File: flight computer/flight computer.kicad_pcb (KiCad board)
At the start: 4 copper layers, 43.2 x 99.1 mm, 153 parts, among them IC1 AT25SF128A-SHB-T, IC2 114993390, IC3 ADXL375BCCZ-RL, J1 JST, J10 Micro_SD_Card, J11 pyro 1, J12 pyro 2, J13 pyro 3, J14 pyro 4, J15 motor out, J16 5V out, J17 motor in, J18 servo 1, J19 servo 2, J2 battery in, J20 servo 3, J21 servo 4, J22 SMA-J-P-H-ST-EM1, J23 SMA-J-P-H-ST-EM1, J3 battery sw, J4 pyro sw, J5 12V out, J6 5V out, J7 3.3V out, J8 USB_C_Receptacle_USB2.0_16P, J9 GPIO, Q3 SIA440DJ-T1-GE3, Q4 SIA440DJ-T1-GE3, Q5 SIA440DJ-T1-GE3, Q6 SIA440DJ-T1-GE3, U1 RP2350B, U10 MAX-M10S-00B, U4 AZ1117CH-3.3TRG1, U5 TPS56A37RPAR, U6 SISS65DN-T1-GE3, U7 BTM9011EP, U8 BMP581, U9 BNO086, Y1 ABM8-272-T3

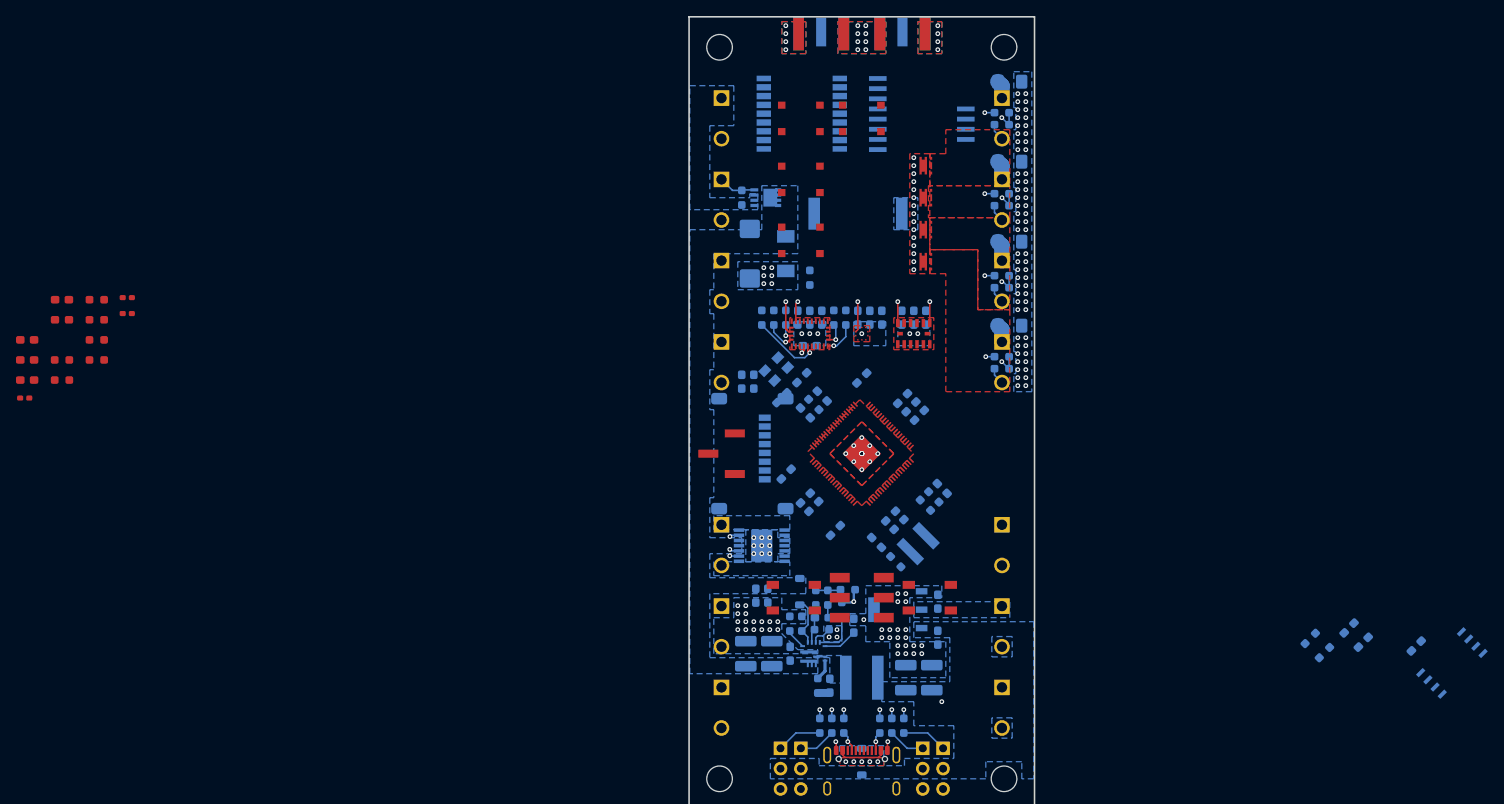
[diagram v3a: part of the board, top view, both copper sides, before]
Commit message: Microcontroller power complete
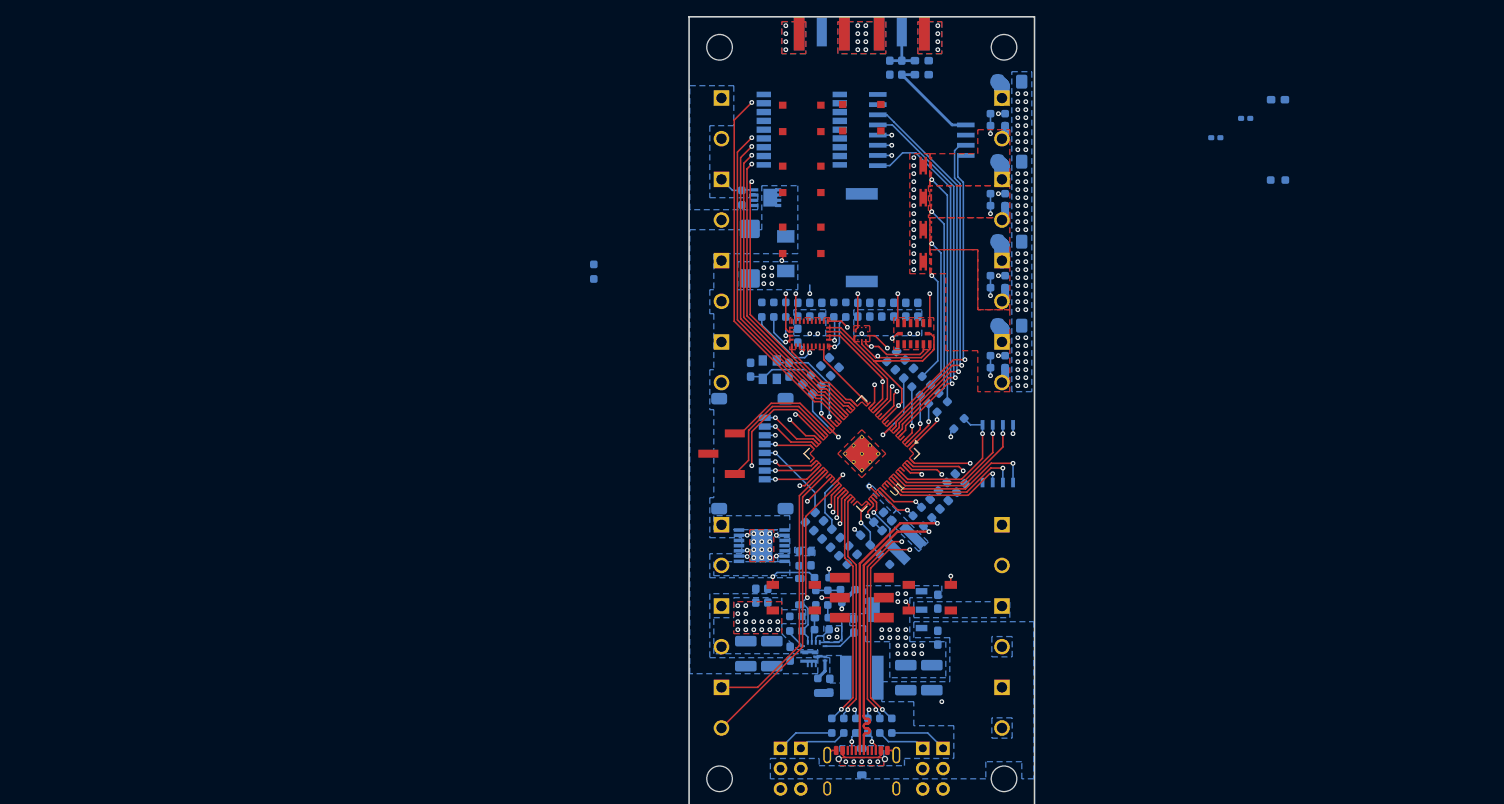
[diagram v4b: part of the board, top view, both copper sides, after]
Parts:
- removed CR3: PESD0402-140, Inductor_SMD:L_0402_1005Metric_Pad0.77x0.64mm_HandSolder
- added D1: D_TVS, Diode_SMD:D_0603_1608Metric_Pad1.05x0.95mm_HandSolder, B.Cu at (201.9, 40.6)
- C40, C43, C52, C54, CR2, L3, L4, R22, R42, R45, R46, R47, R48: moved to B.Cu
- U1: footprint Package_DFN_QFN:QFN-80-1EP_10x10mm_P0.4mm_EP3.4x3.4mm -> Package_DFN_QFN:QFN-80-1EP_10x10mm_P0.4mm_EP3.4x3.4mm_ThermalVias
- Y1: footprint Samacsys:ABM8272T3 -> Snapeda:XTAL_ABM8-272-T3
- moved C43 159.7 mm to (250.4, 44.7), turned to 180 degrees
- moved CR2 156.6 mm to (246.4, 47.0), turned to 180 degrees
- moved R42 154.0 mm to (250.4, 54.7), turned to 180 degrees
- moved L3 137.8 mm to (242.6, 49.4), turned to 180 degrees
- moved C52 118.2 mm to (205.9, 41.5)
- moved C54 111.6 mm to (205.9, 39.8)
- moved L4 109.6 mm to (203.4, 40.6), turned to 90 degrees
- moved R45 106.5 mm to (208.4, 83.0), turned to 45 degrees
- moved R46 105.1 mm to (207.4, 82.0), turned to 45 degrees
- moved R47 103.8 mm to (206.3, 81.0), turned to 45 degrees
- moved R48 102.6 mm to (205.3, 79.9), turned to 45 degrees
- moved C40 101.7 mm to (192.0, 102.0), turned to -90 degrees
- moved R22 95.4 mm to (190.5, 102.0), turned to 90 degrees
- moved C14 71.3 mm to (197.2, 102.1)
- moved R11 63.5 mm to (193.4, 104.4), turned to 0 degrees
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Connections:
- R11 pad 1: Net-(U1-RUN) -> Net-(S2-NO_1)
- R11 pad 2: Net-(S2-NO_1) -> Net-(U1-RUN)
- R7 pad 1: GND -> /QSPI_SS
- R7 pad 2: Net-(S1-COM_1) -> Net-(S1-NO_2)
- S1 pad 2: /QSPI_SS -> Net-(S1-NO_2)
- S1 pad 3: Net-(S1-COM_1) -> GND
- S2 pad 3: unconnected-(S2-COM_1-Pad3) -> GND
- S2 pad 4: GND -> unconnected-(S2-COM_2-Pad4)
- U1 pad 1: unconnected-(U1-GPIO4-Pad1) -> /pyro 1 gate
- U1 pad 11: unconnected-(U1-GPIO12-Pad11) -> /SX1262 int
- U1 pad 13: unconnected-(U1-GPIO14-Pad13) -> /SCK
- U1 pad 14: unconnected-(U1-GPIO15-Pad14) -> /ADXL375 CS
- U1 pad 16: unconnected-(U1-GPIO16-Pad16) -> /BMP581 CS
- U1 pad 17: unconnected-(U1-GPIO17-Pad17) -> /BNO086 CS
- U1 pad 18: unconnected-(U1-GPIO18-Pad18) -> /MOSI
- U1 pad 19: unconnected-(U1-GPIO19-Pad19) -> /MISO
- U1 pad 2: unconnected-(U1-GPIO5-Pad2) -> /pyro 2 gate
- U1 pad 20: unconnected-(U1-GPIO20-Pad20) -> /BNO086 int
- U1 pad 21: unconnected-(U1-GPIO21-Pad21) -> /BNO086 wake
- U1 pad 22: unconnected-(U1-GPIO22-Pad22) -> /MAX M10S boot
- U1 pad 23: unconnected-(U1-GPIO23-Pad23) -> /MAX M10S TX
- U1 pad 25: unconnected-(U1-GPIO24-Pad25) -> /MAX M10S RX
- U1 pad 26: unconnected-(U1-GPIO25-Pad26) -> /MAX M10S timepulse
- U1 pad 27: unconnected-(U1-GPIO26-Pad27) -> /MAX M10S int
- U1 pad 28: unconnected-(U1-GPIO27-Pad28) -> /MAX M10S reset
- U1 pad 3: unconnected-(U1-GPIO6-Pad3) -> /pyro 3 gate
- U1 pad 36: unconnected-(U1-GPIO28-Pad36) -> /buzzer
- U1 pad 37: unconnected-(U1-GPIO29-Pad37) -> /LED controller
- U1 pad 38: unconnected-(U1-GPIO30-Pad38) -> /SD DAT1
- U1 pad 39: unconnected-(U1-GPIO31-Pad39) -> /SD DAT0
- U1 pad 4: unconnected-(U1-GPIO7-Pad4) -> /pyro 4 gate
- U1 pad 40: unconnected-(U1-GPIO32-Pad40) -> /SD CLK
- U1 pad 42: unconnected-(U1-GPIO33-Pad42) -> /SD CMD
- U1 pad 43: unconnected-(U1-GPIO34-Pad43) -> /SD DAT3
- U1 pad 44: unconnected-(U1-GPIO35-Pad44) -> /SD DAT2
- U1 pad 45: unconnected-(U1-GPIO36-Pad45) -> /BTM9011EP CS
- U1 pad 46: unconnected-(U1-GPIO37-Pad46) -> /motor in a
- U1 pad 47: unconnected-(U1-GPIO38-Pad47) -> /motor in b
- U1 pad 49: unconnected-(U1-GPIO40/ADC0-Pad49) -> /BTM9011EP IS
- U1 pad 52: unconnected-(U1-GPIO41/ADC1-Pad52) -> /power signal
- U1 pad 53: unconnected-(U1-GPIO42/ADC2-Pad53) -> /pyro 1 continuity
- U1 pad 54: unconnected-(U1-GPIO43/ADC3-Pad54) -> /pyro 2 continuity
- U1 pad 55: unconnected-(U1-GPIO44/ADC4-Pad55) -> /pyro 3 continuity
- U1 pad 56: unconnected-(U1-GPIO45/ADC5-Pad56) -> /pyro 4 continuity
- U1 pad 57: unconnected-(U1-GPIO46/ADC6-Pad57) -> /servo PWM 1
- U1 pad 58: unconnected-(U1-GPIO47/ADC7-Pad58) -> /servo PWM 2
- U1 pad 6: unconnected-(U1-GPIO8-Pad6) -> /SX1262 rf switch
- U1 pad 7: unconnected-(U1-GPIO9-Pad7) -> /SX1262 reset
- U1 pad 77: unconnected-(U1-GPIO0-Pad77) -> /servo PWM 3
- U1 pad 78: unconnected-(U1-GPIO1-Pad78) -> /servo PWM 4
- U1 pad 79: unconnected-(U1-GPIO2-Pad79) -> /pin out 2
- U1 pad 8: unconnected-(U1-GPIO10-Pad8) -> /SX1262 CS
- U1 pad 80: unconnected-(U1-GPIO3-Pad80) -> /pin out 1
- U1 pad 9: unconnected-(U1-GPIO11-Pad9) -> /SX1262 busy
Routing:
- net /SCK: track 0.00 -> 94.9 mm, vias 0 -> 3
- net /MOSI: track 0.00 -> 84.1 mm, vias 0 -> 4
- net /MISO: track 1.17 -> 81.0 mm, vias 1 -> 5
- net /gate: track 4.70 -> 72.8 mm, vias 0 -> 1
- net /pyro 1 continuity: track 2.77 -> 62.2 mm, vias 1 -> 2
- net /pyro 2 continuity: track 2.86 -> 52.9 mm, vias 1 -> 2
- net /SX1262 CS: track 0.00 -> 48.3 mm, vias 0 -> 1
- net /SX1262 reset: track 0.00 -> 47.1 mm, vias 0 -> 1
- net /MAX M10S reset: track 0.00 -> 46.5 mm, vias 0 -> 1
- net /SX1262 rf switch: track 0.00 -> 45.7 mm, vias 0 -> 1
- net /MAX M10S int: track 0.00 -> 41.6 mm, vias 0 -> 1
- net /SX1262 busy: track 0.00 -> 41.1 mm, vias 0 -> 1
- net /servo PWM 4: track 1.09 -> 41.7 mm, vias 1 -> 3
- net /pyro 3 continuity: track 2.72 -> 43.1 mm, vias 1 -> 2
- net /MAX M10S timepulse: track 0.00 -> 40.0 mm, vias 0 -> 1
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- added copper zone on B.Cu, net +1.1V
- added copper zone on In1.Cu, net +1.1V
- added copper zone on B.Cu, net /BTM9011EP IS
- removed copper zone on F.Cu, net +1.1V
